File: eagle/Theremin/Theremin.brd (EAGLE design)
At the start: 254 x 101.6 mm, 40 parts, among them Q8 2N3904, U1 LM78L12, U2 LM79L12

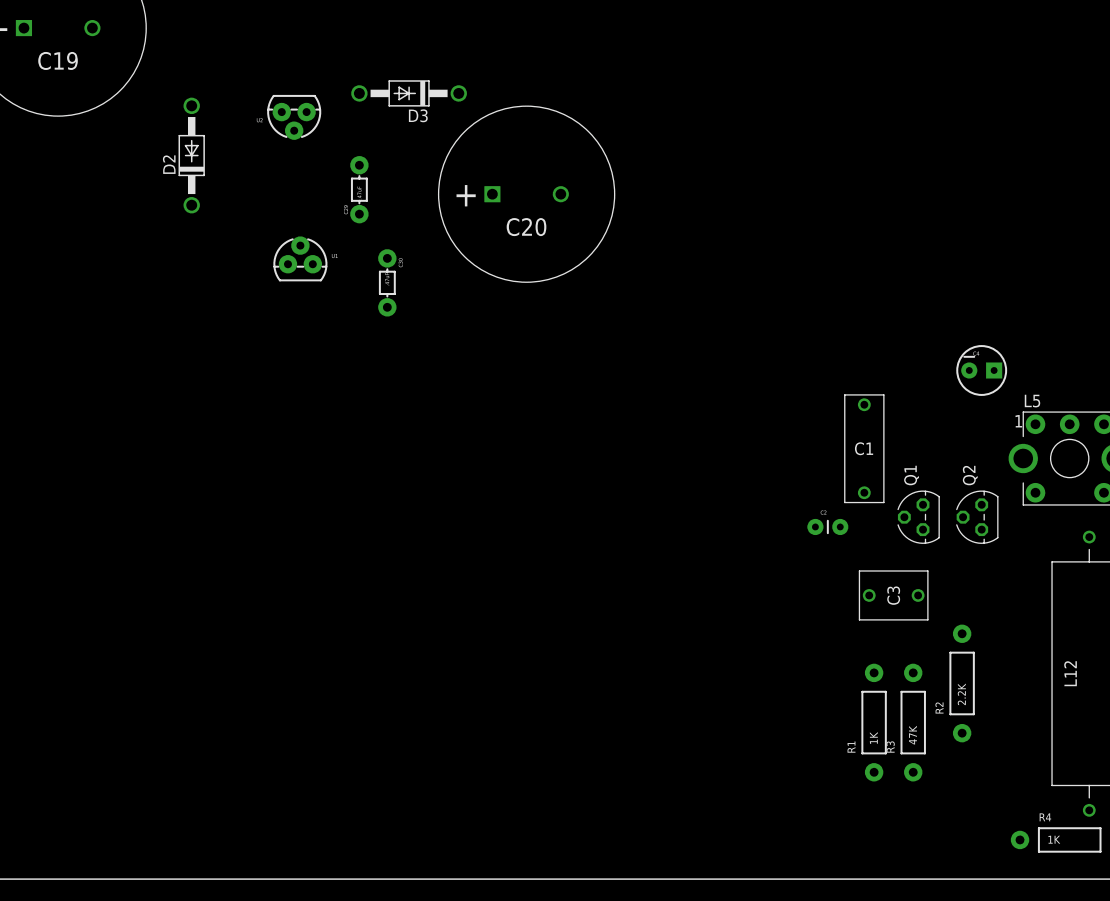
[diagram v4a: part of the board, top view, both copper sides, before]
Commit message: Added LM13600, VCA Processor, headers
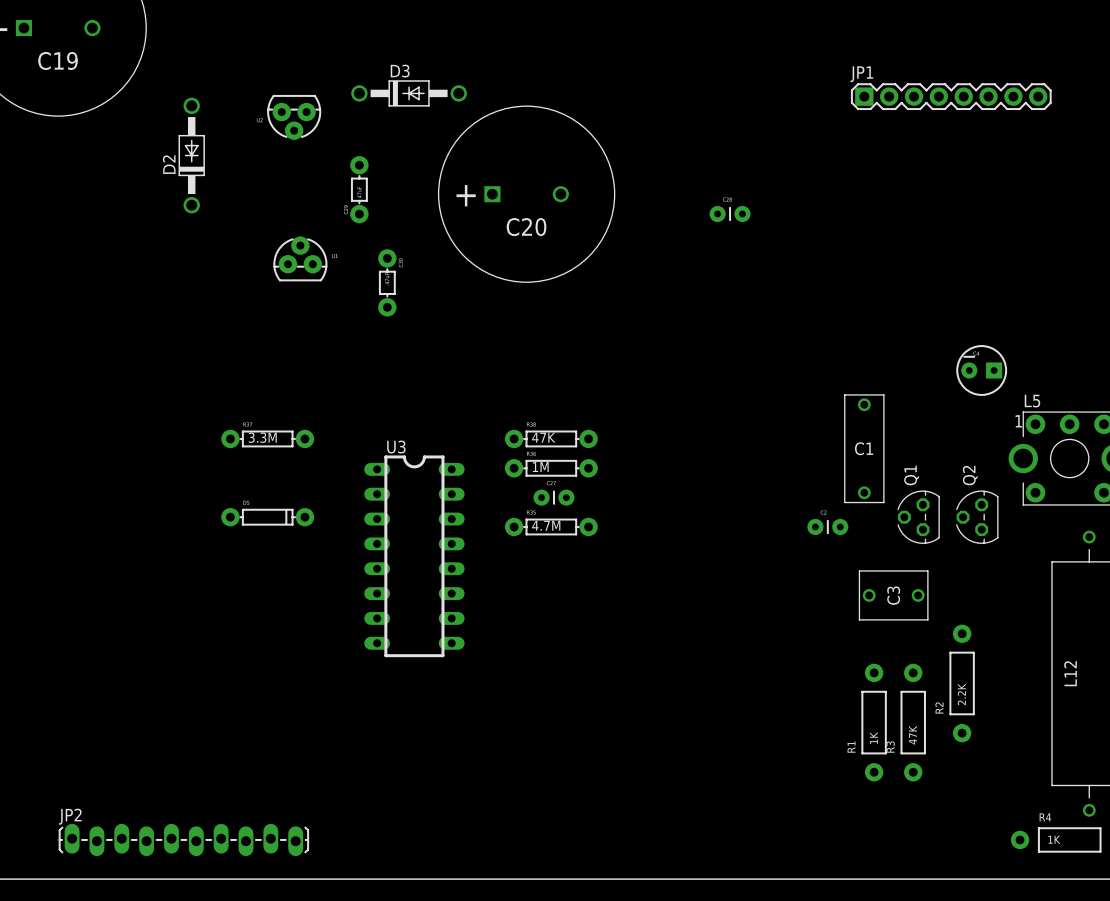
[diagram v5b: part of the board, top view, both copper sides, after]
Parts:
- added C27, C28: 0.1uF, SparkFun-Capacitors:CAP-PTH-SMALL
- added D5: (no value), SparkFun-DiscreteSemi:DIODE-1N4148
- added JP1: (no value), SparkFun-Connectors:1X08
- added JP2: Front Panel, SparkFun-Connectors:1X10_LOCK_LONGPADS
- added R35: 4.7M, SparkFun-Passives:AXIAL-0.3EZ
- added R36: 1M, SparkFun-Passives:AXIAL-0.3EZ
- added R37: 3.3M, SparkFun-Passives:AXIAL-0.3EZ
- added R38: 47K, SparkFun-Passives:AXIAL-0.3EZ
- added U3: (no value), marky-parts:DIL16
- turned D3 to 0 degrees
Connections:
- new net N$21: R38.P$1, U3.16
- new net N$22: JP1.3, U3.10
- new net N$23: JP1.4, U3.9
- new net N$24: C28.1, D5.C, JP1.2, U3.12
- new net N$25: D5.A, R37.P$2
- new net N$26: C27.2, R35.P$1, R37.P$1, U3.13
- new net N$28: R36.P$1, U3.15
- net -12V: now also JP1.5, JP2.3, U3.6
- net 5V: now also JP1.6, JP2.8, R35.P$2, R36.P$2, R38.P$2, U3.11
- net GND: now also C27.1, C28.2, JP1.1, JP2.4, U3.14
- net N$7: now also JP2.6
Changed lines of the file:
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@@
 <element name="L14" library="marky-parts" package="FIXED-INDUCTOR-API-DELEVAN" value="22uH" x="37.45" y="31.1"/>
 <element name="C14" library="SparkFun-Capacitors" package="CAP-PTH-LARGE" value="1800pF" x="23.48" y="26.02" rot="R270"/>
-<element name="D3" library="diode" package="DO41-10" value="1N4004" x="84.455" y="80.3275" rot="R180"/>
+<element name="D3" library="diode" package="DO41-10" value="1N4004" x="84.455" y="80.3275"/>
 <element name="U2" library="marky-parts" package="TO-92" value="LM79L12" x="72.7075" y="78.4225" rot="R180"/>
 <element name="U1" library="marky-parts" package="TO-92" value="LM78L12" x="73.3425" y="62.865"/>
@@
 <element name="C4" library="SparkFun-Passives" package="CPOL-RADIAL-10UF-25V" value="1uF" x="143" y="52"/>
 <element name="C2" library="SparkFun-Capacitors" package="CAP-PTH-SMALL" value="15pF" x="126" y="36"/>
+<element name="U3" library="marky-parts" package="DIL16" value="" x="85" y="33" rot="R270"/>
+<element name="JP1" library="SparkFun-Connectors" package="1X08" value="" x="131" y="80"/>
+<element name="R38" library="SparkFun-Passives" package="AXIAL-0.3EZ" value="47K" x="99" y="45"/>
+<element name="C28" library="SparkFun-Capacitors" package="CAP-PTH-SMALL" value="0.1uF" x="116" y="68"/>
+<element name="D5" library="SparkFun-DiscreteSemi" package="DIODE-1N4148" value="" x="70" y="37"/>
+<element name="R37" library="SparkFun-Passives" package="AXIAL-0.3EZ" value="3.3M" x="70" y="45"/>
+<element name="C27" library="SparkFun-Capacitors" package="CAP-PTH-SMALL" value="0.1uF" x="98" y="39"/>
+<element name="R36" library="SparkFun-Passives" package="AXIAL-0.3EZ" value="1M" x="99" y="42"/>
+<element name="R35" library="SparkFun-Passives" package="AXIAL-0.3EZ" value="4.7M" x="99" y="36"/>
+<element name="JP2" library="SparkFun-Connectors" package="1X10_LOCK_LONGPADS" value="Front Panel" x="50" y="4"/>
 </elements>
 <signals>
@@
 <contactref element="L11" pad="TAB@7"/>
 <contactref element="L11" pad="TAB@8"/>
-<wire x1="147.25" y1="43" x2="156.75" y2="43" width="0" layer="19" extent="1-1"/>
-<wire x1="141.73" y1="52" x2="147.25" y2="43" width="0" layer="19" extent="1-1"/>
-<wire x1="132" y1="10.92" x2="147.25" y2="43" width="0" layer="19" extent="1-1"/>
-<wire x1="157.08" y1="4" x2="132" y2="10.92" width="0" layer="19" extent="1-1"/>
-<wire x1="92.9725" y1="70.025" x2="141.73" y2="52" width="0" layer="19" extent="1-1"/>
+<contactref element="JP1" pad="1"/>
+<contactref element="C28" pad="2"/>
+<contactref element="U3" pad="14"/>
+<contactref element="C27" pad="1"/>
+<contactref element="JP2" pad="4"/>
+<wire x1="118.54" y1="68" x2="131" y2="80" width="0" layer="19" extent="1-1"/>
+<wire x1="92.9725" y1="70.025" x2="118.54" y2="68" width="0" layer="19" extent="1-1"/>
 <wire x1="79.375" y1="67.985" x2="92.9725" y2="70.025" width="0" layer="19" extent="1-1"/>
 <wire x1="73.3425" y1="64.77" x2="79.375" y2="67.985" width="0" layer="19" extent="1-1"/>
@@
 <wire x1="71.4375" y1="78.4225" x2="79.375" y2="67.985" width="0" layer="19" extent="1-1"/>
 <wire x1="52.0775" y1="87.01" x2="71.4375" y2="78.4225" width="0" layer="19" extent="1-1"/>
+<wire x1="88.81" y1="36.81" x2="82.2325" y2="58.46" width="0" layer="19" extent="1-1"/>
+<wire x1="98" y1="39" x2="88.81" y2="36.81" width="0" layer="19" extent="1-1"/>
+<wire x1="141.73" y1="52" x2="118.54" y2="68" width="0" layer="19" extent="1-1"/>
+<wire x1="147.25" y1="43" x2="141.73" y2="52" width="0" layer="19" extent="1-1"/>
+<wire x1="156.75" y1="43" x2="147.25" y2="43" width="0" layer="19" extent="1-1"/>
+<wire x1="132" y1="10.92" x2="147.25" y2="43" width="0" layer="19" extent="1-1"/>
+<wire x1="157.08" y1="4" x2="132" y2="10.92" width="0" layer="19" extent="1-1"/>
 <wire x1="35.85" y1="52.69" x2="52.0775" y2="87.01" width="0" layer="19" extent="1-1"/>
 <wire x1="26.35" y1="52.69" x2="35.85" y2="52.69" width="0" layer="19" extent="1-1"/>
@@
 <wire x1="23.48" y1="17.13" x2="10.78" y2="12.05" width="0" layer="19" extent="1-1"/>
 <wire x1="29" y1="31" x2="23.48" y2="17.13" width="0" layer="19" extent="1-1"/>
+<wire x1="57.62" y1="3.873" x2="10.78" y2="12.05" width="0" layer="19" extent="1-1"/>
 </signal>
 <signal name="N$7">
 <contactref element="R18" pad="P$1"/>
+<contactref element="JP2" pad="6"/>
+<wire x1="62.7" y1="3.873" x2="4.43" y2="18.4" width="0" layer="19" extent="1-1"/>
 </signal>
 <signal name="-12V">
@@
 <contactref element="R16" pad="P$1"/>
 <contactref element="R2" pad="P$1"/>
-<wire x1="23.48" y1="12.05" x2="23.48" y2="14.59" width="0" layer="19" extent="1-1"/>
-<wire x1="23.48" y1="9.51" x2="23.48" y2="12.05" width="0" layer="19" extent="1-1"/>
-<wire x1="141" y1="14.92" x2="23.48" y2="9.51" width="0" layer="19" extent="1-1"/>
+<contactref element="U3" pad="6"/>
+<contactref element="JP1" pad="5"/>
+<contactref element="JP2" pad="3"/>
+<wire x1="141" y1="14.92" x2="141.16" y2="80" width="0" layer="19" extent="1-1"/>
+<wire x1="81.19" y1="29.19" x2="141" y2="14.92" width="0" layer="19" extent="1-1"/>
+<wire x1="55.08" y1="4.127" x2="81.19" y2="29.19" width="0" layer="19" extent="1-1"/>
+<wire x1="23.48" y1="9.51" x2="55.08" y2="4.127" width="0" layer="19" extent="1-1"/>
+<wire x1="23.48" y1="12.05" x2="23.48" y2="9.51" width="0" layer="19" extent="1-1"/>
+<wire x1="23.48" y1="14.59" x2="23.48" y2="12.05" width="0" layer="19" extent="1-1"/>
 </signal>
 <signal name="N$6">
@@
 <contactref element="C29" pad="P$2"/>
 <wire x1="72.7075" y1="76.5175" x2="99.9725" y2="70.025" width="0" layer="19" extent="1-1"/>
-<wire x1="79.375" y1="80.3275" x2="72.7075" y2="76.5175" width="0" layer="19" extent="1-1"/>
-<wire x1="79.375" y1="72.985" x2="79.375" y2="80.3275" width="0" layer="19" extent="1-1"/>
+<wire x1="89.535" y1="80.3275" x2="72.7075" y2="76.5175" width="0" layer="19" extent="1-1"/>
+<wire x1="79.375" y1="72.985" x2="89.535" y2="80.3275" width="0" layer="19" extent="1-1"/>
 </signal>
 <signal name="N$13">
@@
 <contactref element="D3" pad="C"/>
 <contactref element="D2" pad="A"/>
-<wire x1="62.23" y1="79.0575" x2="89.535" y2="80.3275" width="0" layer="19" extent="1-1"/>
+<wire x1="62.23" y1="79.0575" x2="79.375" y2="80.3275" width="0" layer="19" extent="1-1"/>
 </signal>
 <signal name="N$15">
@@
 <contactref element="C4" pad="1"/>
 <contactref element="L5" pad="IN$1"/>
+<contactref element="R38" pad="P$2"/>
+<contactref element="U3" pad="11"/>
+<contactref element="JP1" pad="6"/>
+<contactref element="R36" pad="P$2"/>
+<contactref element="R35" pad="P$2"/>
+<contactref element="JP2" pad="8"/>
+<wire x1="144.27" y1="52" x2="143.7" y2="80" width="0" layer="19" extent="1-1"/>
+<wire x1="148.5" y1="46.5" x2="144.27" y2="52" width="0" layer="19" extent="1-1"/>
 <wire x1="143" y1="38.27" x2="148.5" y2="46.5" width="0" layer="19" extent="1-1"/>
 <wire x1="136.5" y1="29" x2="143" y2="38.27" width="0" layer="19" extent="1-1"/>
-<wire x1="131" y1="48.5" x2="148.5" y2="46.5" width="0" layer="19" extent="1-1"/>
-<wire x1="29.83" y1="41.26" x2="131" y2="48.5" width="0" layer="19" extent="1-1"/>
+<wire x1="136" y1="21.08" x2="136.5" y2="29" width="0" layer="19" extent="1-1"/>
+<wire x1="131" y1="48.5" x2="144.27" y2="52" width="0" layer="19" extent="1-1"/>
+<wire x1="102.81" y1="45" x2="131" y2="48.5" width="0" layer="19" extent="1-1"/>
+<wire x1="102.81" y1="42" x2="102.81" y2="45" width="0" layer="19" extent="1-1"/>
+<wire x1="102.81" y1="36" x2="102.81" y2="42" width="0" layer="19" extent="1-1"/>
+<wire x1="88.81" y1="29.19" x2="102.81" y2="36" width="0" layer="19" extent="1-1"/>
+<wire x1="67.78" y1="3.873" x2="88.81" y2="29.19" width="0" layer="19" extent="1-1"/>
+<wire x1="29.83" y1="41.26" x2="67.78" y2="3.873" width="0" layer="19" extent="1-1"/>
 <wire x1="27.6" y1="56.19" x2="29.83" y2="41.26" width="0" layer="19" extent="1-1"/>
 <wire x1="18.4" y1="51.42" x2="27.6" y2="56.19" width="0" layer="19" extent="1-1"/>
-<wire x1="136" y1="21.08" x2="29.83" y2="41.26" width="0" layer="19" extent="1-1"/>
-<wire x1="144.27" y1="52" x2="136" y2="21.08" width="0" layer="19" extent="1-1"/>
 </signal>
 <signal name="N$17">
@@
 <contactref element="C2" pad="2"/>
 </signal>
+<signal name="N$21">
+<contactref element="U3" pad="16"/>
+<contactref element="R38" pad="P$1"/>
+<wire x1="88.81" y1="41.89" x2="95.19" y2="45" width="0" layer="19" extent="1-1"/>
+</signal>
+<signal name="N$22">
+<contactref element="U3" pad="10"/>
+<contactref element="JP1" pad="3"/>
+<wire x1="136.08" y1="80" x2="88.81" y2="26.65" width="0" layer="19" extent="1-1"/>
+</signal>
+<signal name="N$23">
+<contactref element="U3" pad="9"/>
+<contactref element="JP1" pad="4"/>
+<wire x1="138.62" y1="80" x2="88.81" y2="24.11" width="0" layer="19" extent="1-1"/>
+</signal>
+<signal name="N$24">
+<contactref element="U3" pad="12"/>
+<contactref element="C28" pad="1"/>
+<contactref element="JP1" pad="2"/>
+<contactref element="D5" pad="C"/>
+<wire x1="88.81" y1="31.73" x2="133.54" y2="80" width="0" layer="19" extent="1-1"/>
+<wire x1="73.81" y1="37" x2="88.81" y2="31.73" width="0" layer="19" extent="1-1"/>
+<wire x1="116" y1="68" x2="73.81" y2="37" width="0" layer="19" extent="1-1"/>
+</signal>
+<signal name="N$25">
+<contactref element="D5" pad="A"/>
+<contactref element="R37" pad="P$2"/>
+<wire x1="73.81" y1="45" x2="66.19" y2="37" width="0" layer="19" extent="1-1"/>
+</signal>
+<signal name="N$26">
+<contactref element="R37" pad="P$1"/>
+<contactref element="C27" pad="2"/>
+<contactref element="U3" pad="13"/>
+<contactref element="R35" pad="P$1"/>
+<wire x1="100.54" y1="39" x2="88.81" y2="34.27" width="0" layer="19" extent="1-1"/>
+<wire x1="66.19" y1="45" x2="100.54" y2="39" width="0" layer="19" extent="1-1"/>
+<wire x1="95.19" y1="36" x2="100.54" y2="39" width="0" layer="19" extent="1-1"/>
+</signal>
+<signal name="N$28">
+<contactref element="U3" pad="15"/>
+<contactref element="R36" pad="P$1"/>
+<wire x1="95.19" y1="42" x2="88.81" y2="39.35" width="0" layer="19" extent="1-1"/>
+</signal>
 </signals>

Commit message: Work on VOLTAGE CONTROLLED AMPLIFIER section
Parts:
- added C25: 1uF, SparkFun-Passives:CPOL-RADIAL-10UF-25V
- added C26: 0.01uF, marky-parts:5M-CAP-RADIAL
- added R29: 100K, SparkFun-Resistors:AXIAL-0.4
- added R30: 47K, SparkFun-Resistors:AXIAL-0.4
- added R32, R33, R34: 4.7M, SparkFun-Passives:AXIAL-0.3EZ
- moved D5 2.00 mm to (70.0, 39.0)
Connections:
- new net N$27: R29.P$2, R30.P$1, U3.1
- new net N$29: C25.2, R32.P$2, U3.8
- new net N$30: C25.1, R33.P$1
- new net N$31: C26.P$2, JP2.10, R33.P$2, R34.P$1
- net -12V: now also R29.P$1, R32.P$1
- net GND: now also C26.P$1, R34.P$2
- net N$24: now also R30.P$2
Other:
- board size 254 x 101.6 mm -> 161 x 101.6 mm
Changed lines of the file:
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@@
 <board>
 <plain>
-<wire x1="0" y1="0" x2="254" y2="0" width="0" layer="20"/>
-<wire x1="254" y1="0" x2="254" y2="101.6" width="0" layer="20"/>
-<wire x1="254" y1="101.6" x2="0" y2="101.6" width="0" layer="20"/>
+<wire x1="0" y1="0" x2="161" y2="0" width="0" layer="20"/>
+<wire x1="161" y1="0" x2="161" y2="101.6" width="0" layer="20"/>
+<wire x1="161" y1="101.6" x2="0" y2="101.6" width="0" layer="20"/>
 <wire x1="0" y1="101.6" x2="0" y2="0" width="0" layer="20"/>
 <text x="5.08" y="96.52" size="1.778" layer="51">Marky's House</text>
@@
 <element name="R38" library="SparkFun-Passives" package="AXIAL-0.3EZ" value="47K" x="99" y="45"/>
 <element name="C28" library="SparkFun-Capacitors" package="CAP-PTH-SMALL" value="0.1uF" x="116" y="68"/>
-<element name="D5" library="SparkFun-DiscreteSemi" package="DIODE-1N4148" value="" x="70" y="37"/>
+<element name="D5" library="SparkFun-DiscreteSemi" package="DIODE-1N4148" value="" x="70" y="39"/>
 <element name="R37" library="SparkFun-Passives" package="AXIAL-0.3EZ" value="3.3M" x="70" y="45"/>
 <element name="C27" library="SparkFun-Capacitors" package="CAP-PTH-SMALL" value="0.1uF" x="98" y="39"/>
@@
 <element name="R35" library="SparkFun-Passives" package="AXIAL-0.3EZ" value="4.7M" x="99" y="36"/>
 <element name="JP2" library="SparkFun-Connectors" package="1X10_LOCK_LONGPADS" value="Front Panel" x="50" y="4"/>
+<element name="R30" library="SparkFun-Resistors" package="AXIAL-0.4" value="47K" x="70" y="42"/>
+<element name="R29" library="SparkFun-Resistors" package="AXIAL-0.4" value="100K" x="70" y="36"/>
+<element name="R32" library="SparkFun-Passives" package="AXIAL-0.3EZ" value="4.7M" x="69" y="14"/>
+<element name="C25" library="SparkFun-Passives" package="CPOL-RADIAL-10UF-25V" value="1uF" x="77" y="8"/>
+<element name="R33" library="SparkFun-Passives" package="AXIAL-0.3EZ" value="4.7M" x="87" y="11"/>
+<element name="C26" library="marky-parts" package="5M-CAP-RADIAL" value="0.01uF" x="88" y="5"/>
+<element name="R34" library="SparkFun-Passives" package="AXIAL-0.3EZ" value="4.7M" x="87" y="16"/>
 </elements>
 <signals>
@@
 <contactref element="C27" pad="1"/>
 <contactref element="JP2" pad="4"/>
+<contactref element="C26" pad="P$1"/>
+<contactref element="R34" pad="P$2"/>
 <wire x1="118.54" y1="68" x2="131" y2="80" width="0" layer="19" extent="1-1"/>
 <wire x1="92.9725" y1="70.025" x2="118.54" y2="68" width="0" layer="19" extent="1-1"/>
@@
 <wire x1="23.48" y1="17.13" x2="10.78" y2="12.05" width="0" layer="19" extent="1-1"/>
 <wire x1="29" y1="31" x2="23.48" y2="17.13" width="0" layer="19" extent="1-1"/>
-<wire x1="57.62" y1="3.873" x2="10.78" y2="12.05" width="0" layer="19" extent="1-1"/>
+<wire x1="88" y1="7.5" x2="10.78" y2="12.05" width="0" layer="19" extent="1-1"/>
+<wire x1="90.81" y1="16" x2="88" y2="7.5" width="0" layer="19" extent="1-1"/>
+<wire x1="57.62" y1="3.873" x2="23.48" y2="17.13" width="0" layer="19" extent="1-1"/>
 </signal>
 <signal name="N$7">
@@
 <contactref element="JP1" pad="5"/>
 <contactref element="JP2" pad="3"/>
+<contactref element="R32" pad="P$1"/>
+<contactref element="R29" pad="P$1"/>
 <wire x1="141" y1="14.92" x2="141.16" y2="80" width="0" layer="19" extent="1-1"/>
 <wire x1="81.19" y1="29.19" x2="141" y2="14.92" width="0" layer="19" extent="1-1"/>
@@
 <wire x1="23.48" y1="12.05" x2="23.48" y2="9.51" width="0" layer="19" extent="1-1"/>
 <wire x1="23.48" y1="14.59" x2="23.48" y2="12.05" width="0" layer="19" extent="1-1"/>
+<wire x1="64.92" y1="36" x2="23.48" y2="9.51" width="0" layer="19" extent="1-1"/>
+<wire x1="65.19" y1="14" x2="64.92" y2="36" width="0" layer="19" extent="1-1"/>
 </signal>
 <signal name="N$6">
@@
 <contactref element="JP1" pad="2"/>
 <contactref element="D5" pad="C"/>
-<wire x1="88.81" y1="31.73" x2="133.54" y2="80" width="0" layer="19" extent="1-1"/>
-<wire x1="73.81" y1="37" x2="88.81" y2="31.73" width="0" layer="19" extent="1-1"/>
-<wire x1="116" y1="68" x2="73.81" y2="37" width="0" layer="19" extent="1-1"/>
+<contactref element="R30" pad="P$2"/>
+<wire x1="116" y1="68" x2="133.54" y2="80" width="0" layer="19" extent="1-1"/>
+<wire x1="88.81" y1="31.73" x2="116" y2="68" width="0" layer="19" extent="1-1"/>
+<wire x1="73.81" y1="39" x2="88.81" y2="31.73" width="0" layer="19" extent="1-1"/>
+<wire x1="75.08" y1="42" x2="73.81" y2="39" width="0" layer="19" extent="1-1"/>
 </signal>
 <signal name="N$25">
 <contactref element="D5" pad="A"/>
 <contactref element="R37" pad="P$2"/>
-<wire x1="73.81" y1="45" x2="66.19" y2="37" width="0" layer="19" extent="1-1"/>
+<wire x1="73.81" y1="45" x2="66.19" y2="39" width="0" layer="19" extent="1-1"/>
 </signal>
 <signal name="N$26">
@@
 <wire x1="95.19" y1="42" x2="88.81" y2="39.35" width="0" layer="19" extent="1-1"/>
 </signal>
+<signal name="N$27">
+<contactref element="U3" pad="1"/>
+<contactref element="R30" pad="P$1"/>
+<contactref element="R29" pad="P$2"/>
+<wire x1="75.08" y1="36" x2="81.19" y2="41.89" width="0" layer="19" extent="1-1"/>
+<wire x1="64.92" y1="42" x2="75.08" y2="36" width="0" layer="19" extent="1-1"/>
+</signal>
+<signal name="N$29">
+<contactref element="U3" pad="8"/>
+<contactref element="R32" pad="P$2"/>
+<contactref element="C25" pad="2"/>
+<wire x1="72.81" y1="14" x2="81.19" y2="24.11" width="0" layer="19" extent="1-1"/>
+<wire x1="75.73" y1="8" x2="72.81" y2="14" width="0" layer="19" extent="1-1"/>
+</signal>
+<signal name="N$30">
+<contactref element="R33" pad="P$1"/>
+<contactref element="C25" pad="1"/>
+<wire x1="78.27" y1="8" x2="83.19" y2="11" width="0" layer="19" extent="1-1"/>
+</signal>
+<signal name="N$31">
+<contactref element="R33" pad="P$2"/>
+<contactref element="JP2" pad="10"/>
+<contactref element="C26" pad="P$2"/>
+<contactref element="R34" pad="P$1"/>
+<wire x1="90.81" y1="11" x2="72.86" y2="3.873" width="0" layer="19" extent="1-1"/>
+<wire x1="88" y1="2.5" x2="90.81" y2="11" width="0" layer="19" extent="1-1"/>
+<wire x1="83.19" y1="16" x2="88" y2="2.5" width="0" layer="19" extent="1-1"/>
+</signal>
 </signals>
